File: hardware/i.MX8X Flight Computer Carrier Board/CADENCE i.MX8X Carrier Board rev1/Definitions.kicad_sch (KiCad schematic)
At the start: 8 parts, among them U37 TXS0101DCKR, U38 TXS0101DCKR, U43 TXS0101DCKR, U44 TXS0101DCKR

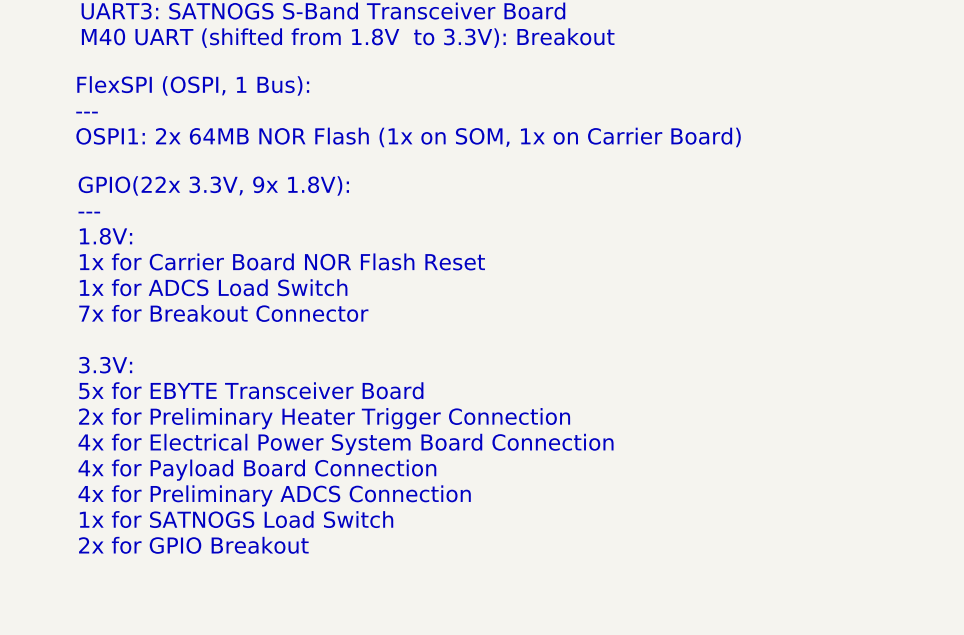
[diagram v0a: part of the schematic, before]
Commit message: more debug header pins
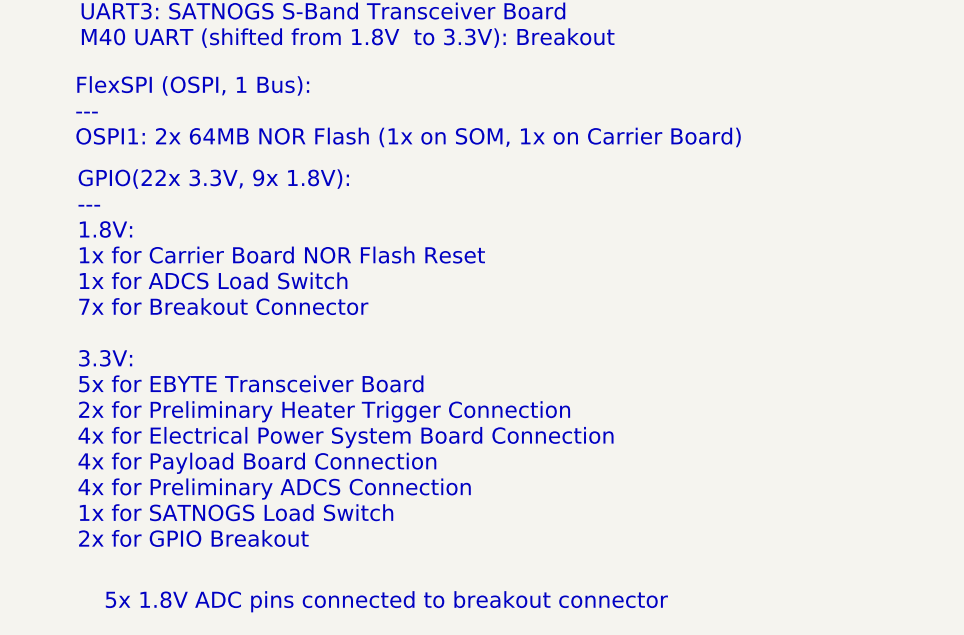
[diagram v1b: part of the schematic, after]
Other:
- note added: "5x 1.8V ADC pins connected to breakout connector"
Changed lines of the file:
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@@
+		)
+	)
+	(text "5x 1.8V ADC pins connected to breakout connector"
+		(exclude_from_sim no)
+		(at 47.498 188.468 0)
+		(effects
+			(font
+				(size 1.778 1.778)
+			)
 		)
 	)
@@
 	(text "GPIO(22x 3.3V, 9x 1.8V):\n---\n1.8V:\n1x for Carrier Board NOR Flash Reset\n1x for ADCS Load Switch\n7x for Breakout Connector\n\n3.3V:\n5x for EBYTE Transceiver Board\n2x for Preliminary Heater Trigger Connection\n4x for Electrical Power System Board Connection\n4x for Payload Board Connection\n4x for Preliminary ADCS Connection\n1x for SATNOGS Load Switch\n2x for GPIO Breakout\n\n"
 		(exclude_from_sim no)
-		(at 13.208 163.83 0)
+		(at 13.208 163.068 0)
 		(effects
 			(font

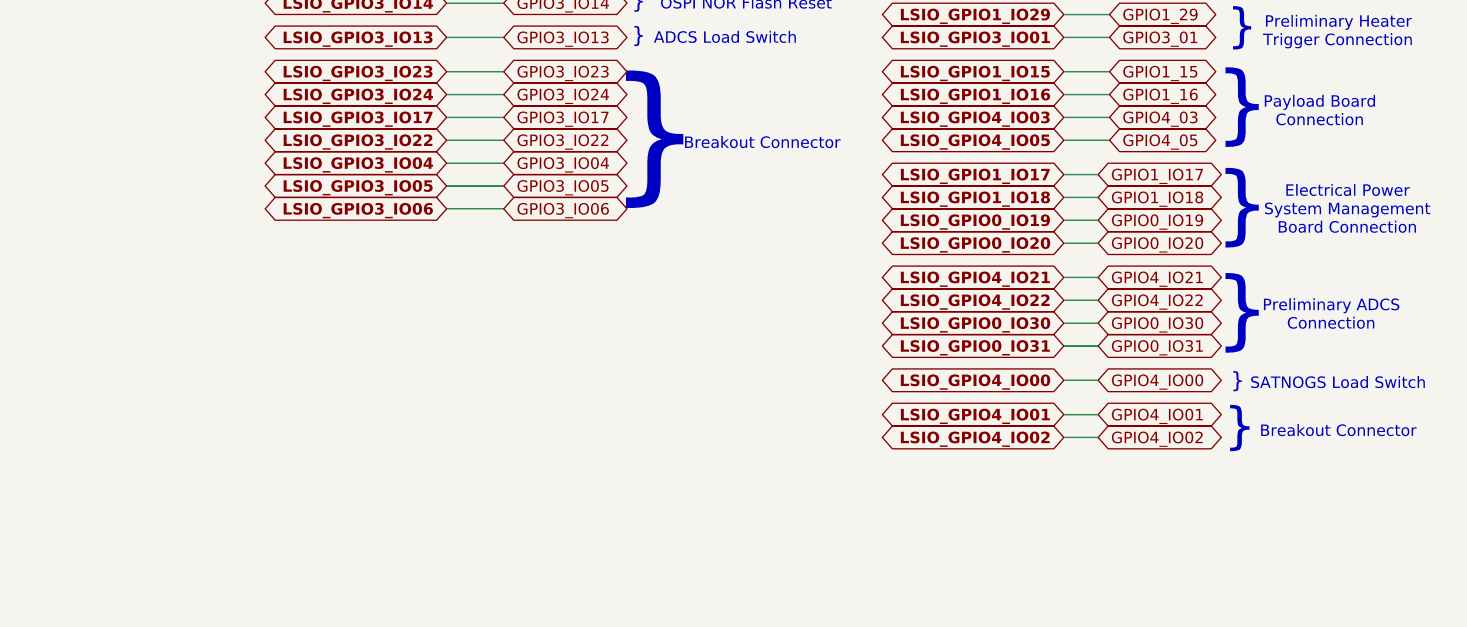
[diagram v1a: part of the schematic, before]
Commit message: connection changes, debug headers, fixing critical issues
-finished debug/utility header pin section (may have to reassign some gpios again tho)
- added can bus transceiver and connection to satnogs
- reassigned/ ensured no i2c address conflict
- resolved critical error in LTC-3115 power regulator symbol where output power was shorted to sync pin
-resolved critical symbol issue in which imx8x som power good symbol shorted to gnd, which would result in nonfunctional board & 2 jtag pins shorted

to do:
- assign gpio to a load switch
- resolve erc issues
- footprint check (shunt resistor change, some new ics need footprints, cmos image sensor 8 pin jst connector, etc)
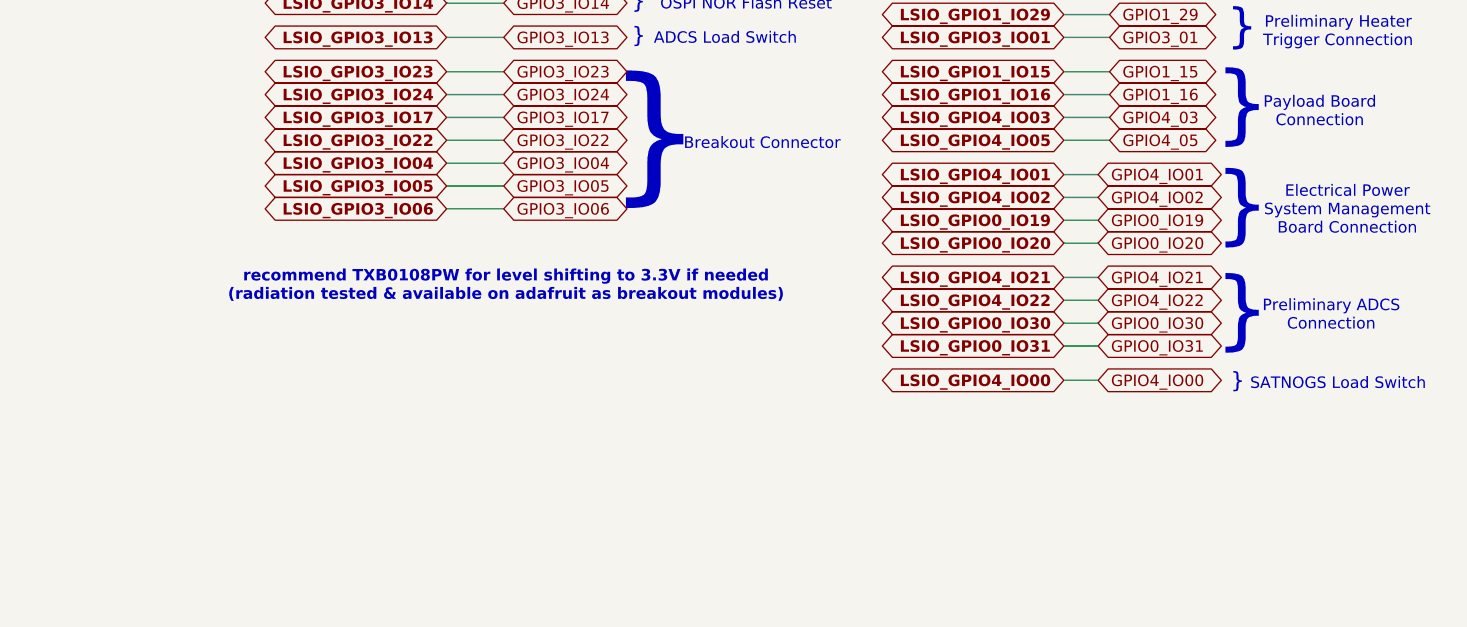
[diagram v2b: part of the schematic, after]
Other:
- note added: "recommend TXB0108PW for level shifting to 3.3V if needed (radiation tested & available on adafruit as breakout modules)"
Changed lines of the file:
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@@
 		)
 	)
-	(text "(Ebyte Transceiver)"
+	(text "recommend TXB0108PW for level shifting to 3.3V if needed\n(radiation tested & available on adafruit as breakout modules)"
 		(exclude_from_sim no)
-		(at 147.828 165.608 0)
+		(at 180.594 116.586 0)
 		(effects
 			(font
-				(size 2.54 2.54)
+				(size 1.27 1.27)
+				(thickness 0.254)
+				(bold yes)
 			)
 		)
 	)
-	(text "}"
+	(text "(Ebyte Transceiver)"
 		(exclude_from_sim no)
-		(at 262.382 107.696 0)
+		(at 147.828 165.608 0)
 		(effects
 			(font
-				(size 6.985 6.985)
+				(size 2.54 2.54)
 			)
 		)
@@
 	(text "}"
 		(exclude_from_sim no)
-		(at 262.128 132.334 0)
+		(at 262.382 107.696 0)
 		(effects
 			(font
-				(size 4.064 4.064)
+				(size 6.985 6.985)
 			)
 		)
@@
 		)
 	)
-	(text "Breakout Connector"
-		(exclude_from_sim no)
-		(at 273.05 132.842 0)
-		(effects
-			(font
-				(size 1.27 1.27)
-			)
-		)
-	)
 	(text "}"
 		(exclude_from_sim no)
@@
 	(wire
 		(pts
-			(xy 242.57 104.14) (xy 246.38 104.14)
-		)
-		(stroke
-			(width 0)
-			(type default)
-		)
-	)
-	(wire
-		(pts
 			(xy 228.6 31.75) (xy 228.6 30.48)
 		)
@@
 	(wire
 		(pts
-			(xy 242.57 106.68) (xy 246.38 106.68)
-		)
-		(stroke
-			(width 0)
-			(type default)
-		)
-	)
-	(wire
-		(pts
 			(xy 193.04 36.83) (xy 201.93 36.83)
 		)
@@
 	(wire
 		(pts
-			(xy 242.57 133.35) (xy 246.38 133.35)
+			(xy 242.57 106.68) (xy 246.38 106.68)
 		)
 		(stroke
@@
 	(wire
 		(pts
-			(xy 242.57 130.81) (xy 246.38 130.81)
+			(xy 242.57 104.14) (xy 246.38 104.14)
 		)
 		(stroke
@@
 	(global_label "GPIO4_IO02"
 		(shape bidirectional)
-		(at 246.38 133.35 0)
+		(at 246.38 106.68 0)
 		(fields_autoplaced yes)
 		(effects
@@
 		)
 		(property "Intersheetrefs" "${INTERSHEET_REFS}"
-			(at 261.4832 133.35 0)
+			(at 261.4832 106.68 0)
 			(effects
 				(font
@@
 		)
 	)
-	(global_label "GPIO1_IO17"
-		(shape bidirectional)
-		(at 246.38 104.14 0)
-		(fields_autoplaced yes)
-		(effects
-			(font
-				(size 1.27 1.27)
-			)
-			(justify left)
-		)
-		(property "Intersheetrefs" "${INTERSHEET_REFS}"
-			(at 261.4832 104.14 0)
-			(effects
-				(font
-					(size 1.27 1.27)
-				)
-				(justify left)
-				(hide yes)
-			)
-		)
-	)
 	(global_label "GPIO1_25"
 		(shape bidirectional)
@@
 	(global_label "LSIO_GPIO4_IO01"
 		(shape bidirectional)
-		(at 242.57 130.81 180)
+		(at 242.57 104.14 180)
 		(fields_autoplaced yes)
 		(effects
@@
 		)
 		(property "Intersheetrefs" "${INTERSHEET_REFS}"
-			(at 221.8503 130.81 0)
+			(at 221.8503 104.14 0)
 			(effects
 				(font
@@
 		)
 	)
-	(global_label "LSIO_GPIO1_IO18"
-		(shape bidirectional)
-		(at 242.57 106.68 180)
-		(fields_autoplaced yes)
-		(effects
-			(font
-				(size 1.27 1.27)
-				(thickness 0.254)
-				(bold yes)
-			)
-			(justify right)
-		)
-		(property "Intersheetrefs" "${INTERSHEET_REFS}"
-			(at 221.8503 106.68 0)
-			(effects
-				(font
-					(size 1.27 1.27)
-				)
-				(justify right)
-				(hide yes)
-			)
-		)
-	)
 	(global_label "LSIO_GPIO0_IO31"
 		(shape bidirectional)
@@
 		)
 	)
-	(global_label "LSIO_GPIO1_IO17"
-		(shape bidirectional)
-		(at 242.57 104.14 180)
-		(fields_autoplaced yes)
-		(effects
-			(font
-				(size 1.27 1.27)
-				(thickness 0.254)
-				(bold yes)
-			)
-			(justify right)
-		)
-		(property "Intersheetrefs" "${INTERSHEET_REFS}"
-			(at 221.8503 104.14 0)
-			(effects
-				(font
-					(size 1.27 1.27)
-				)
-				(justify right)
-				(hide yes)
-			)
-		)
-	)
 	(global_label "GPIO4_05"
 		(shape bidirectional)
@@
 		)
 	)
-	(global_label "GPIO1_IO18"
-		(shape bidirectional)
-		(at 246.38 106.68 0)
-		(fields_autoplaced yes)
-		(effects
-			(font
-				(size 1.27 1.27)
-			)
-			(justify left)
-		)
-		(property "Intersheetrefs" "${INTERSHEET_REFS}"
-			(at 261.4832 106.68 0)
-			(effects
-				(font
-					(size 1.27 1.27)
-				)
-				(justify left)
-				(hide yes)
-			)
-		)
-	)
 	(global_label "X_M40_UART0_TX_1V8"
 		(shape bidirectional)
@@
 	(global_label "GPIO4_IO01"
 		(shape bidirectional)
-		(at 246.38 130.81 0)
+		(at 246.38 104.14 0)
 		(fields_autoplaced yes)
 		(effects
@@
 		)
 		(property "Intersheetrefs" "${INTERSHEET_REFS}"
-			(at 261.4832 130.81 0)
+			(at 261.4832 104.14 0)
 			(effects
 				(font
@@
 	(global_label "LSIO_GPIO4_IO02"
 		(shape bidirectional)
-		(at 242.57 133.35 180)
+		(at 242.57 106.68 180)
 		(fields_autoplaced yes)
 		(effects
@@
 		)
 		(property "Intersheetrefs" "${INTERSHEET_REFS}"
-			(at 221.8503 133.35 0)
+			(at 221.8503 106.68 0)
 			(effects
 				(font

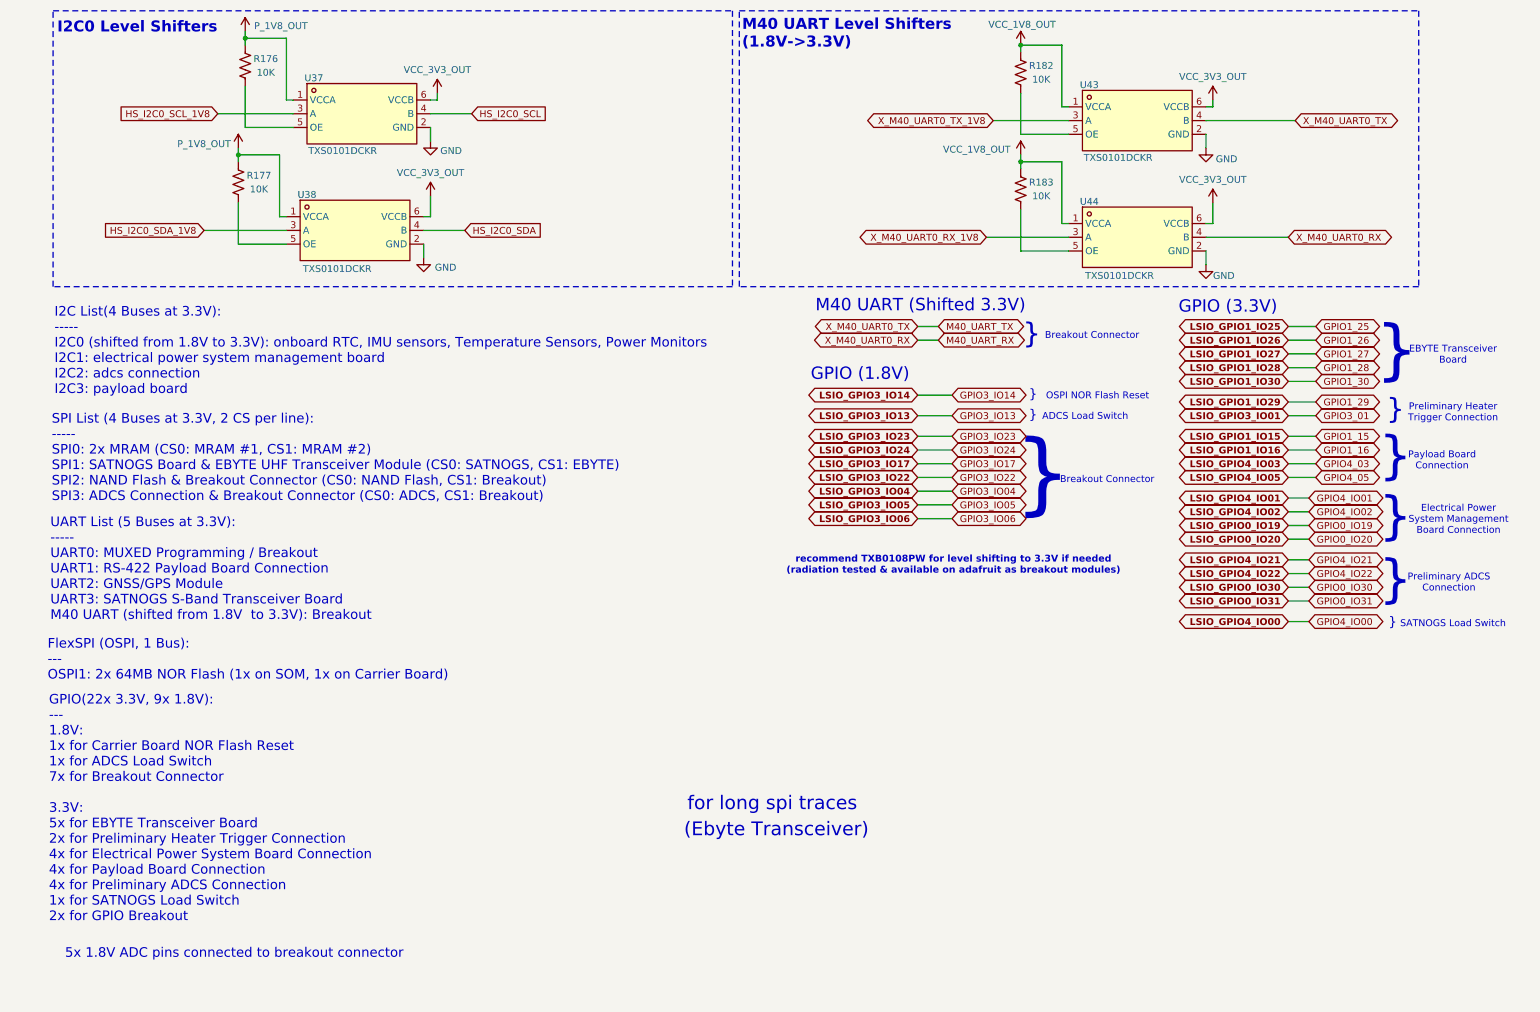
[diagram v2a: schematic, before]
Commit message: Some ERC fixes, schematic annotations, pinmux for uSD & GPIO fixes, GPIO level shifter, footprint selection & pathway fix
component footprints for most part have been selected
going to double check again tmr
imx8x som bth samtec connector footprint needs to be adjusted as reference footprint uses each connector as individual symbol, while we have as part of one symbol (spacing between connector is important so som can fit in)
also one component didnt have part (uart mux) and havent assigned
implemented can bus interface with satnogs, moved around gpios, level shifted 8 gpios, fixed few missing connections (gps 1pps, a load switch enable gpio), resolved some erc errors/ symbol shorts, incorrect pinmux implementation around A9&10 for uSD and gpio, reannotated schematic, fixed footprint reference paths
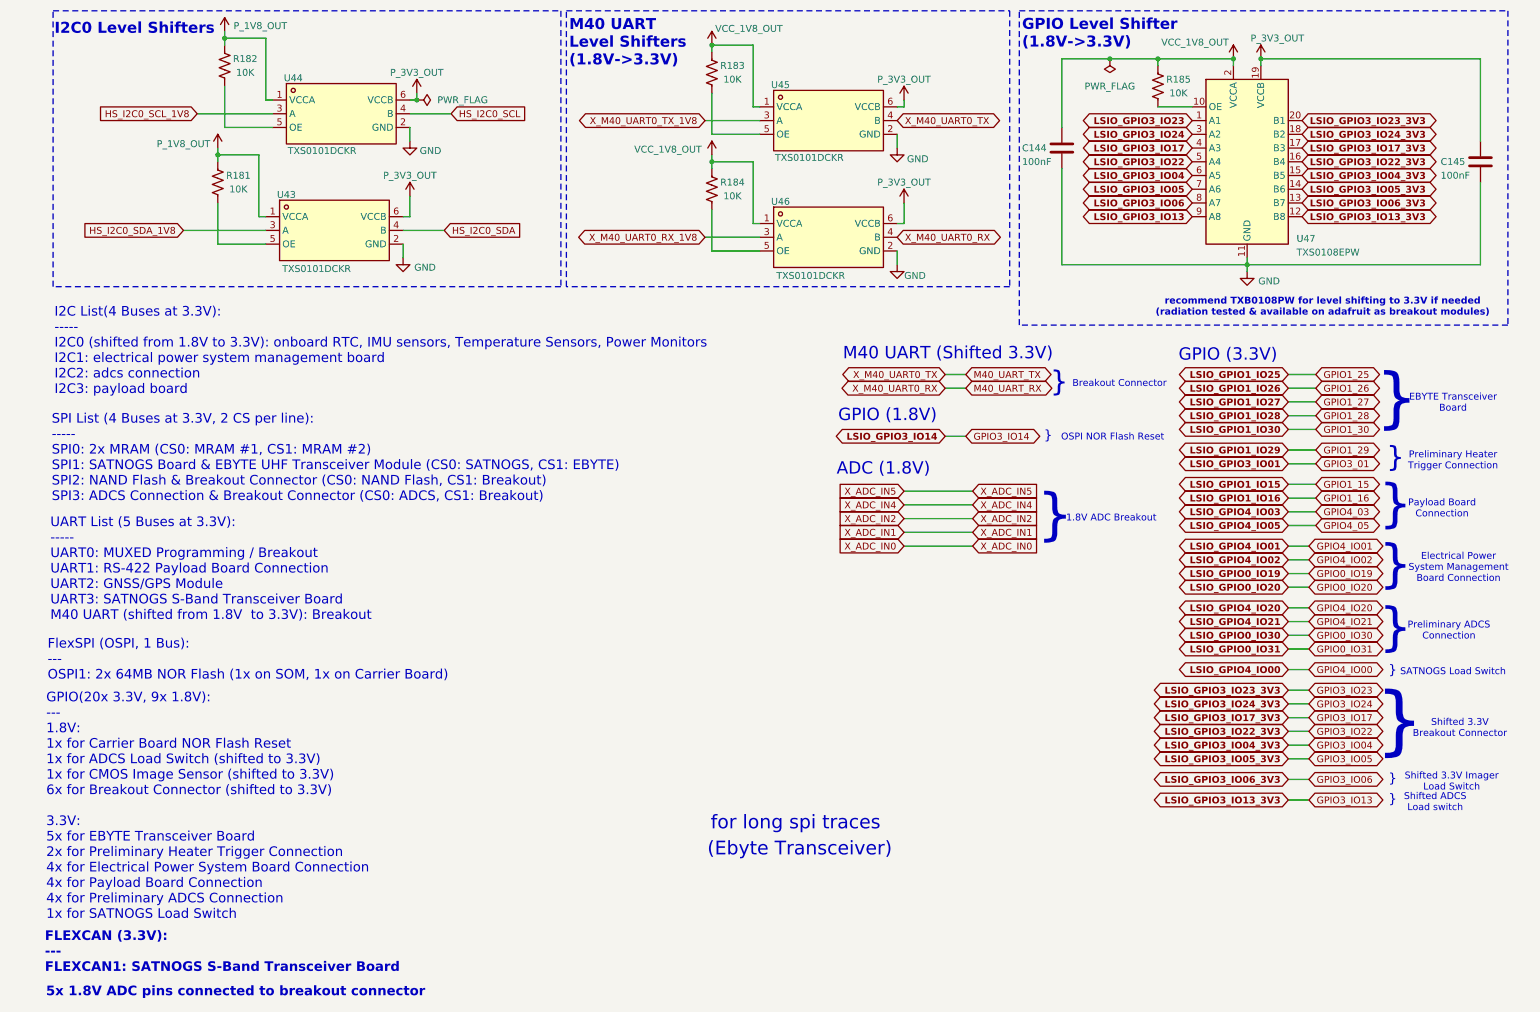
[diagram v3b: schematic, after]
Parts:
- added C144, C145: 100nF, Capacitor_SMD:C_0402_1005Metric, symbol Device:C
- added R185: 10K, Resistor_SMD:R_0402_1005Metric, symbol Device:R_US
- added U47: TXS0108EPW, Package_SO:TSSOP-20_4.4x6.5mm_P0.65mm, symbol Logic_LevelTranslator:TXS0108EPW
- renumbered R177 to R181, R176 to R182, R182 to R183, R183 to R184, U38 to U43, U37 to U44, U43 to U45, U44 to U46
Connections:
- net GND: now also C144.2, C145.2, U47.11 (GND)
- net GPIO3_IO04: now also U47.15 (B5)
- net GPIO3_IO05: now also U47.14 (B6)
- net GPIO3_IO06: now also U47.13 (B7)
- net GPIO3_IO13: now also U47.12 (B8)
- net GPIO3_IO17: now also U47.17 (B3)
- net GPIO3_IO22: now also U47.16 (B4)
- net GPIO3_IO23: now also U47.20 (B1)
- net GPIO3_IO24: now also U47.18 (B2)
- net VCC_1V8_OUT: now also C144.1, R185.1, U47.2 (VCCA)
- net VCC_3V3_OUT renamed P_3V3_OUT
- net P_3V3_OUT: now also C145.1, U47.19 (VCCB)
- new net: R185.2, U47.10 (OE)
- new net LSIO_GPIO3_IO04: U47.6 (A5)
- new net LSIO_GPIO3_IO05: U47.7 (A6)
- new net LSIO_GPIO3_IO06: U47.8 (A7)
- new net LSIO_GPIO3_IO13: U47.9 (A8)
- new net LSIO_GPIO3_IO17: U47.4 (A3)
- new net LSIO_GPIO3_IO22: U47.5 (A4)
- new net LSIO_GPIO3_IO23: U47.1 (A1)
- new net LSIO_GPIO3_IO24: U47.3 (A2)
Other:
- note added: "1.8V ADC Breakout"
- note added: "ADC (1.8V)"
- note added: "FLEXCAN (3.3V): --- FLEXCAN1: SATNOGS S-Band Transceiver Board"
- note added: "GPIO Level Shifter (1.8V->3.3V)"
- note added: "GPIO(20x 3.3V, 9x 1.8V): --- 1.8V: 1x for Carrier Board NOR Flash Reset 1x for ADCS Load Switch (shifted to 3.3V) 1x for CMOS Image Sensor (shifted to 3.3V) 6x for Breakout Connector (shifted to 3.3V) 3.3V: 5x for EBYTE Transceiver Board 2x for Preliminary Heater Trigger Connection 4x for Electrical Power System Board Connection 4x for Payload Board Connection 4x for Preliminary ADCS Connection 1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"
- note added: "Shifted 3.3V Breakout Connector"
- note added: "Shifted 3.3V Imager Load Switch"
- note added: "Shifted ADCS Load switch"
- note removed: "ADCS Load Switch"
- note removed: "GPIO(22x 3.3V, 9x 1.8V): --- 1.8V: 1x for Carrier Board NOR Flash Reset 1x for ADCS Load Switch 7x for Breakout Connector 3.3V: 5x for EBYTE Transceiver Board 2x for Preliminary Heater Trigger Connection 4x for Electrical Power System Board Connection 4x for Payload Board Connection 4x for Preliminary ADCS Connection 1x for SATNOGS Load Switch 2x for GPIO Breakout"
- moved on the sheet: R181, R182, R183, R184, U43, U44, U45, U46
